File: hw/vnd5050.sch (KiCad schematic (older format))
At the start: 5 parts, among them U401 VND5050AJTR-E

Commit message: making 2.2.0 pcb
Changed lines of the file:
@@
 $Descr A4 11693 8268
 encoding utf-8
-Sheet 6 6
+Sheet 8 8
 Title ""
 Date ""
@@
 AR Path="/5A02A41F/59D8088A" Ref="U901"  Part="1"
 AR Path="/5A07C729/59D8088A" Ref="U901"  Part="1"
-F 0 "U901" H 4700 4447 60  0000 C CNN
+AR Path="/5A337B26/59D8088A" Ref="U801"  Part="1"
+F 0 "U801" H 4700 4447 60  0000 C CNN
 F 1 "VND5050AJTR-E" H 4700 4341 60  0000 C CNN
 F 2 "usevolt:PowerSSO-12" H 4600 4400 60  0001 C CNN
@@
 AR Path="/5A015FC0/59D808C7" Ref="#PWR019"  Part="1"
 AR Path="/5A02A41F/59D808C7" Ref="#PWR029"  Part="1"
-AR Path="/5A07C729/59D808C7" Ref="#PWR602"  Part="1"
-F 0 "#PWR602" H 5250 3500 50  0001 C CNN
+AR Path="/5A07C729/59D808C7" Ref="#PWR502"  Part="1"
+AR Path="/5A337B26/59D808C7" Ref="#PWR702"  Part="1"
+F 0 "#PWR702" H 5250 3500 50  0001 C CNN
 F 1 "VDD" H 5267 3823 50  0000 C CNN
 F 2 "" H 5250 3650 50  0000 C CNN
@@
 AR Path="/5A015FC0/59D86DC2" Ref="#PWR020"  Part="1"
 AR Path="/5A02A41F/59D86DC2" Ref="#PWR030"  Part="1"
-AR Path="/5A07C729/59D86DC2" Ref="#PWR601"  Part="1"
-F 0 "#PWR601" H 3600 4200 50  0001 C CNN
+AR Path="/5A07C729/59D86DC2" Ref="#PWR501"  Part="1"
+AR Path="/5A337B26/59D86DC2" Ref="#PWR701"  Part="1"
+F 0 "#PWR701" H 3600 4200 50  0001 C CNN
 F 1 "GND" H 3605 4277 50  0000 C CNN
 F 2 "" H 3600 4450 50  0000 C CNN
@@
 AR Path="/5A02A41F/59D88771" Ref="R902"  Part="1"
 AR Path="/5A07C729/59D88771" Ref="R902"  Part="1"
-F 0 "R902" H 3850 4284 45  0000 C CNN
+AR Path="/5A337B26/59D88771" Ref="R804"  Part="1"
+F 0 "R804" H 3850 4284 45  0000 C CNN
 F 1 "390" H 3850 4200 45  0000 C CNN
 F 2 "yageo:0603" H 3830 4250 20  0001 C CNN
@@
 AR Path="/5A02A41F/59D88845" Ref="R901"  Part="1"
 AR Path="/5A07C729/59D88845" Ref="R901"  Part="1"
-F 0 "R901" H 3850 4084 45  0000 C CNN
+AR Path="/5A337B26/59D88845" Ref="R803"  Part="1"
+F 0 "R803" H 3850 4084 45  0000 C CNN
 F 1 "390" H 3850 4000 45  0000 C CNN
 F 2 "yageo:0603" H 3830 4050 20  0001 C CNN
@@
 AR Path="/5A02A41F/5A05950C" Ref="R903"  Part="1"
 AR Path="/5A07C729/5A05950C" Ref="R903"  Part="1"
-F 0 "R903" H 3450 4084 45  0000 C CNN
+AR Path="/5A337B26/5A05950C" Ref="R801"  Part="1"
+F 0 "R801" H 3450 4084 45  0000 C CNN
 F 1 "1K" H 3450 4000 45  0000 C CNN
 F 2 "yageo:0603" H 3430 4050 20  0001 C CNN
@@
 AR Path="/5A02A41F/5A059568" Ref="R904"  Part="1"
 AR Path="/5A07C729/5A059568" Ref="R904"  Part="1"
-F 0 "R904" H 3450 4284 45  0000 C CNN
+AR Path="/5A337B26/5A059568" Ref="R802"  Part="1"
+F 0 "R802" H 3450 4284 45  0000 C CNN
 F 1 "1K" H 3450 4200 45  0000 C CNN
 F 2 "yageo:0603" H 3430 4250 20  0001 C CNN

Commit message: 3.0.0 hw with low side heater mosfet
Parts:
- R401, R402: symbol 390 -> fsb-rescue:390
- R403, R404: symbol 1K -> fsb-rescue:1K
- U401: symbol VND5050AJTR-E -> fsb-rescue:VND5050AJTR-E
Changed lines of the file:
@@
-EESchema Schematic File Version 2
-LIBS:fsb-rescue
-LIBS:kemet
-LIBS:power
-LIBS:usevolt
-LIBS:wurth_elektronik_LED
-LIBS:yageo
+EESchema Schematic File Version 4
 LIBS:fsb-cache
 EELAYER 26 0
@@
 SENSE2
 $Comp
-L VND5050AJTR-E U401
+L fsb-rescue:VND5050AJTR-E U401
 U 1 1 59D8088A
 P 4600 4000
@@
 $EndComp
 $Comp
-L VDD #PWR019
+L fsb-rescue:VDD #PWR019
 U 1 1 59D808C7
 P 5250 3650
 AR Path="/5A015FC0/59D808C7" Ref="#PWR019"  Part="1"
 AR Path="/5A02A41F/59D808C7" Ref="#PWR029"  Part="1"
-AR Path="/5A07C729/59D808C7" Ref="#PWR502"  Part="1"
-AR Path="/5A337B26/59D808C7" Ref="#PWR702"  Part="1"
-F 0 "#PWR702" H 5250 3500 50  0001 C CNN
+AR Path="/5A07C729/59D808C7" Ref="#PWR0502"  Part="1"
+AR Path="/5A337B26/59D808C7" Ref="#PWR0702"  Part="1"
+F 0 "#PWR0702" H 5250 3500 50  0001 C CNN
 F 1 "VDD" H 5267 3823 50  0000 C CNN
 F 2 "" H 5250 3650 50  0000 C CNN
@@
 	3200 4000 4300 4000
 $Comp
-L GND #PWR020
+L fsb-rescue:GND #PWR020
 U 1 1 59D86DC2
 P 3600 4450
 AR Path="/5A015FC0/59D86DC2" Ref="#PWR020"  Part="1"
 AR Path="/5A02A41F/59D86DC2" Ref="#PWR030"  Part="1"
-AR Path="/5A07C729/59D86DC2" Ref="#PWR501"  Part="1"
-AR Path="/5A337B26/59D86DC2" Ref="#PWR701"  Part="1"
-F 0 "#PWR701" H 3600 4200 50  0001 C CNN
+AR Path="/5A07C729/59D86DC2" Ref="#PWR0501"  Part="1"
+AR Path="/5A337B26/59D86DC2" Ref="#PWR0701"  Part="1"
+F 0 "#PWR0701" H 3600 4200 50  0001 C CNN
 F 1 "GND" H 3605 4277 50  0000 C CNN
 F 2 "" H 3600 4450 50  0000 C CNN
@@
 	3600 4300 4300 4300
 $Comp
-L 390 R402
+L fsb-rescue:390 R402
 U 1 1 59D88771
 P 3800 4100
@@
 $EndComp
 $Comp
-L 390 R401
+L fsb-rescue:390 R401
 U 1 1 59D88845
 P 3800 3900
@@
 Connection ~ 4150 3900
 $Comp
-L 1K R403
+L fsb-rescue:1K R403
 U 1 1 5A05950C
 P 3400 3900
@@
 $EndComp
 $Comp
-L 1K R404
+L fsb-rescue:1K R404
 U 1 1 5A059568
 P 3400 4100

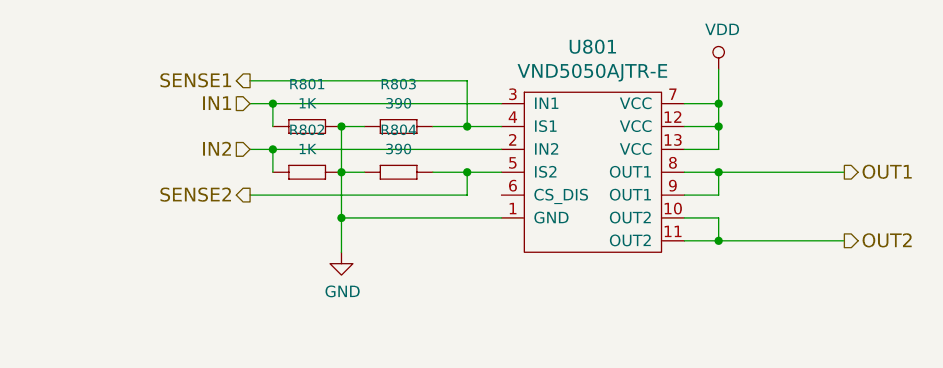
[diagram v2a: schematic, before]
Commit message: HAL updated to latest uv bootloader, starting to draw 6.0.0 pcb
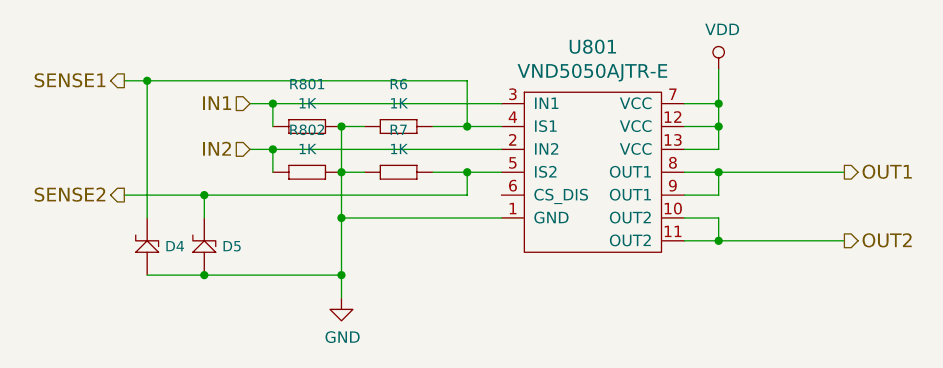
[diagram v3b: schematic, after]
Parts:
- removed R401, R402: 390, yageo:0603, symbol fsb-rescue:390
- added D2, D3: ZENER_MM3Z3V6T1G, usevolt:SOD-323, symbol usevolt:ZENER_MM3Z3V6T1G
- added R1, R2: 1K, yageo:0603, symbol fsb-rescue:1K
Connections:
- net GND: now also D2.2, D3.2, R1.2 (R2), R2.2 (R2)
- net SENSE1: now also D2.1, R1.1 (R1)
- net SENSE2: now also D3.1, R2.1 (R1)
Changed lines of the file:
@@
 $Descr A4 11693 8268
 encoding utf-8
-Sheet 8 8
+Sheet 5 8
 Title ""
 Date ""
@@
 Text HLabel 3200 4000 0    60   Input ~ 0
 IN2
-Text HLabel 3200 3700 0    60   Output ~ 0
+Text HLabel 2650 3700 0    60   Output ~ 0
 SENSE1
-Text HLabel 3200 4200 0    60   Output ~ 0
+Text HLabel 2650 4200 0    60   Output ~ 0
 SENSE2
 $Comp
@@
 $EndComp
 Wire Wire Line
-	5250 3650 5250 4000
+	5250 3650 5250 3800
 Wire Wire Line
 	5250 3800 5100 3800
@@
 Connection ~ 5250 3900
 Wire Wire Line
-	5100 4100 5800 4100
+	5100 4100 5250 4100
 Wire Wire Line
 	5100 4200 5250 4200
@@
 Connection ~ 5250 4100
 Wire Wire Line
-	5100 4400 5800 4400
+	5100 4400 5250 4400
 Wire Wire Line
 	5100 4300 5250 4300
@@
 Connection ~ 5250 4400
 Wire Wire Line
-	3200 3800 4300 3800
-Wire Wire Line
-	3200 4000 4300 4000
+	3200 3800 3300 3800
+Wire Wire Line
+	3200 4000 3300 4000
 $Comp
 L fsb-rescue:GND #PWR020
 U 1 1 59D86DC2
-P 3600 4450
+P 3600 4650
 AR Path="/5A015FC0/59D86DC2" Ref="#PWR020"  Part="1"
 AR Path="/5A02A41F/59D86DC2" Ref="#PWR030"  Part="1"
 AR Path="/5A07C729/59D86DC2" Ref="#PWR0501"  Part="1"
 AR Path="/5A337B26/59D86DC2" Ref="#PWR0701"  Part="1"
-F 0 "#PWR0701" H 3600 4200 50  0001 C CNN
-F 1 "GND" H 3605 4277 50  0000 C CNN
-F 2 "" H 3600 4450 50  0000 C CNN
-F 3 "" H 3600 4450 50  0000 C CNN
-	1    3600 4450
-	1    0    0    -1
-$EndComp
-Wire Wire Line
-	3600 3900 3600 4450
+F 0 "#PWR0701" H 3600 4400 50  0001 C CNN
+F 1 "GND" H 3605 4477 50  0000 C CNN
+F 2 "" H 3600 4650 50  0000 C CNN
+F 3 "" H 3600 4650 50  0000 C CNN
+	1    3600 4650
+	1    0    0    -1
+$EndComp
+Wire Wire Line
+	3600 3900 3600 4100
 Wire Wire Line
 	3600 4300 4300 4300
-$Comp
-L fsb-rescue:390 R402
-U 1 1 59D88771
-P 3800 4100
-AR Path="/5A015FC0/59D88771" Ref="R402"  Part="1"
-AR Path="/5A02A41F/59D88771" Ref="R902"  Part="1"
-AR Path="/5A07C729/59D88771" Ref="R902"  Part="1"
-AR Path="/5A337B26/59D88771" Ref="R804"  Part="1"
-F 0 "R804" H 3850 4284 45  0000 C CNN
-F 1 "390" H 3850 4200 45  0000 C CNN
-F 2 "yageo:0603" H 3830 4250 20  0001 C CNN
-F 3 "" H 3769 4139 60  0001 C CNN
-F 4 "" H 4169 4539 60  0001 C CNN "1st Source Part Number"
-F 5 "Digikey" H 4069 4439 60  0001 C CNN "1st Source"
-F 6 "RC0603FR-07390RL" H 3969 4339 60  0001 C CNN "Manufacturer Part Number"
-F 7 "YAGEO" H 3869 4239 60  0001 C CNN "Manufacturer"
-	1    3800 4100
-	1    0    0    -1
-$EndComp
-$Comp
-L fsb-rescue:390 R401
-U 1 1 59D88845
-P 3800 3900
-AR Path="/5A015FC0/59D88845" Ref="R401"  Part="1"
-AR Path="/5A02A41F/59D88845" Ref="R901"  Part="1"
-AR Path="/5A07C729/59D88845" Ref="R901"  Part="1"
-AR Path="/5A337B26/59D88845" Ref="R803"  Part="1"
-F 0 "R803" H 3850 4084 45  0000 C CNN
-F 1 "390" H 3850 4000 45  0000 C CNN
-F 2 "yageo:0603" H 3830 4050 20  0001 C CNN
-F 3 "" H 3769 3939 60  0001 C CNN
-F 4 "" H 4169 4339 60  0001 C CNN "1st Source Part Number"
-F 5 "Digikey" H 4069 4239 60  0001 C CNN "1st Source"
-F 6 "RC0603FR-07390RL" H 3969 4139 60  0001 C CNN "Manufacturer Part Number"
-F 7 "YAGEO" H 3869 4039 60  0001 C CNN "Manufacturer"
-	1    3800 3900
-	1    0    0    -1
-$EndComp
 Wire Wire Line
 	3700 3900 3600 3900
@@
 Connection ~ 3600 4100
 Wire Wire Line
-	4000 4100 4300 4100
-Wire Wire Line
-	4000 3900 4300 3900
-Wire Wire Line
-	3200 4200 4150 4200
+	4000 4100 4150 4100
+Wire Wire Line
+	4000 3900 4150 3900
+Wire Wire Line
+	2650 4200 3000 4200
 Wire Wire Line
 	4150 4200 4150 4100
@@
 	4150 3900 4150 3700
 Wire Wire Line
-	4150 3700 3200 3700
+	4150 3700 2750 3700
 Connection ~ 4150 3900
 $Comp
@@
 Connection ~ 3300 4000
 Connection ~ 3600 3900
+Wire Wire Line
+	5250 3800 5250 3900
+Wire Wire Line
+	5250 3900 5250 4000
+Wire Wire Line
+	5250 4100 5800 4100
+Wire Wire Line
+	5250 4400 5800 4400
+Wire Wire Line
+	3600 4300 3600 4550
+Wire Wire Line
+	3600 4100 3600 4300
+Wire Wire Line
+	4150 4100 4300 4100
+Wire Wire Line
+	4150 3900 4300 3900
+Wire Wire Line
+	3300 3800 4300 3800
+Wire Wire Line
+	3300 4000 4300 4000
+$Comp
+L fsb-rescue:1K R?
+U 1 1 5C01EA8C
+P 3800 4100
+AR Path="/5A015FC0/5C01EA8C" Ref="R?"  Part="1"
+AR Path="/5A02A41F/5C01EA8C" Ref="R?"  Part="1"
+AR Path="/5A07C729/5C01EA8C" Ref="R2"  Part="1"
+AR Path="/5A337B26/5C01EA8C" Ref="R7"  Part="1"
+F 0 "R7" H 3850 4284 45  0000 C CNN
+F 1 "1K" H 3850 4200 45  0000 C CNN
+F 2 "yageo:0603" H 3830 4250 20  0001 C CNN
+F 3 "" H 3769 4139 60  0001 C CNN
+F 4 "" H 4169 4539 60  0001 C CNN "1st Source Part Number"
+F 5 "Digikey" H 4069 4439 60  0001 C CNN "1st Source"
+F 6 "RC0603FR-071KL" H 3969 4339 60  0001 C CNN "Manufacturer Part Number"
+F 7 "YAGEO" H 3869 4239 60  0001 C CNN "Manufacturer"
+	1    3800 4100
+	1    0    0    -1
+$EndComp
+$Comp
+L fsb-rescue:1K R?
+U 1 1 5C01EABC
+P 3800 3900
+AR Path="/5A015FC0/5C01EABC" Ref="R?"  Part="1"
+AR Path="/5A02A41F/5C01EABC" Ref="R?"  Part="1"
+AR Path="/5A07C729/5C01EABC" Ref="R1"  Part="1"
+AR Path="/5A337B26/5C01EABC" Ref="R6"  Part="1"
+F 0 "R6" H 3850 4084 45  0000 C CNN
+F 1 "1K" H 3850 4000 45  0000 C CNN
+F 2 "yageo:0603" H 3830 4050 20  0001 C CNN
+F 3 "" H 3769 3939 60  0001 C CNN
+F 4 "" H 4169 4339 60  0001 C CNN "1st Source Part Number"
+F 5 "Digikey" H 4069 4239 60  0001 C CNN "1st Source"
+F 6 "RC0603FR-071KL" H 3969 4139 60  0001 C CNN "Manufacturer Part Number"
+F 7 "YAGEO" H 3869 4039 60  0001 C CNN "Manufacturer"
+	1    3800 3900
+	1    0    0    -1
+$EndComp
+$Comp
+L usevolt:ZENER_MM3Z3V6T1G D2
+U 1 1 5C0230BD
+P 2750 4350
+AR Path="/5A07C729/5C0230BD" Ref="D2"  Part="1"
+AR Path="/5A337B26/5C0230BD" Ref="D4"  Part="1"
+F 0 "D4" V 2675 4272 45  0000 R CNN
+F 1 "ZENER_MM3Z3V6T1G" H 3025 4725 45  0001 L BNN
+F 2 "usevolt:SOD-323" H 2725 4725 20  0001 C CNN
+F 3 "http://www.mouser.com/ds/2/308/MM3Z2V4T1-D-269162.pdf" H 3100 4925 60  0001 C CNN
+F 4 "Mouser" H 3070 4670 60  0001 C CNN "1st Source"
+F 5 "MM3Z3V6T1G" H 2970 4570 60  0001 C CNN "Manufacturer Part Number"
+F 6 "863-MM3Z3V6T1G" H 3170 4770 60  0001 C CNN "1st Source Part Number"
+F 7 "ON Semiconductor" H 3025 4825 60  0001 C CNN "Manufacturer"
+	1    2750 4350
+	0    -1   -1   0
+$EndComp
+$Comp
+L usevolt:ZENER_MM3Z3V6T1G D3
+U 1 1 5C023146
+P 3000 4350
+AR Path="/5A07C729/5C023146" Ref="D3"  Part="1"
+AR Path="/5A337B26/5C023146" Ref="D5"  Part="1"
+F 0 "D5" V 2925 4272 45  0000 R CNN
+F 1 "ZENER_MM3Z3V6T1G" H 3275 4725 45  0001 L BNN
+F 2 "usevolt:SOD-323" H 2975 4725 20  0001 C CNN
+F 3 "http://www.mouser.com/ds/2/308/MM3Z2V4T1-D-269162.pdf" H 3350 4925 60  0001 C CNN
+F 4 "Mouser" H 3320 4670 60  0001 C CNN "1st Source"
+F 5 "MM3Z3V6T1G" H 3220 4570 60  0001 C CNN "Manufacturer Part Number"
+F 6 "863-MM3Z3V6T1G" H 3420 4770 60  0001 C CNN "1st Source Part Number"
+F 7 "ON Semiconductor" H 3275 4825 60  0001 C CNN "Manufacturer"
+	1    3000 4350
+	0    -1   -1   0
+$EndComp
+Wire Wire Line
+	3000 4300 3000 4200
+Connection ~ 3000 4200
+Wire Wire Line
+	3000 4200 4150 4200
+Wire Wire Line
+	2750 4300 2750 3700
+Connection ~ 2750 3700
+Wire Wire Line
+	2750 3700 2650 3700
+Wire Wire Line
+	2750 4550 3000 4550
+Wire Wire Line
+	3000 4550 3600 4550
+Connection ~ 3000 4550
+Connection ~ 3600 4550
+Wire Wire Line
+	3600 4550 3600 4650
 $EndSCHEMATC

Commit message: coolvalve added to fsb
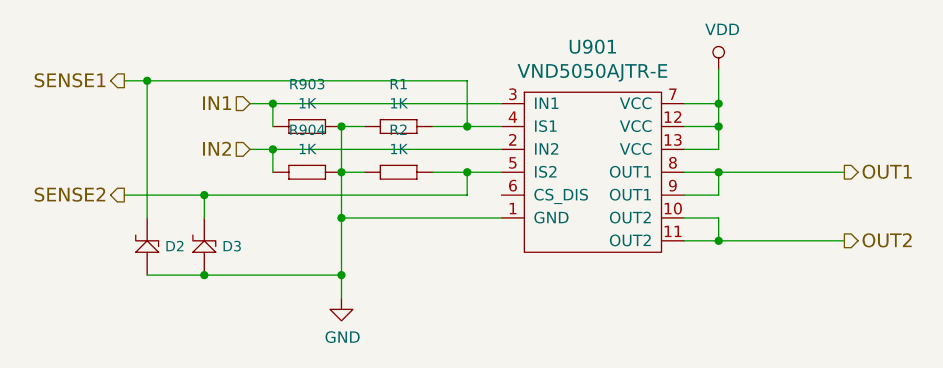
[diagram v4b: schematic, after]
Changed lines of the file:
@@
 $Descr A4 11693 8268
 encoding utf-8
-Sheet 5 8
+Sheet 5 9
 Title ""
 Date ""
@@
 AR Path="/5A07C729/59D8088A" Ref="U901"  Part="1"
 AR Path="/5A337B26/59D8088A" Ref="U801"  Part="1"
-F 0 "U801" H 4700 4447 60  0000 C CNN
+AR Path="/5F353556/59D8088A" Ref="U4"  Part="1"
+F 0 "U901" H 4700 4447 60  0000 C CNN
 F 1 "VND5050AJTR-E" H 4700 4341 60  0000 C CNN
 F 2 "usevolt:PowerSSO-12" H 4600 4400 60  0001 C CNN
@@
 AR Path="/5A07C729/59D808C7" Ref="#PWR0502"  Part="1"
 AR Path="/5A337B26/59D808C7" Ref="#PWR0702"  Part="1"
-F 0 "#PWR0702" H 5250 3500 50  0001 C CNN
+AR Path="/5F353556/59D808C7" Ref="#PWR0116"  Part="1"
+F 0 "#PWR0502" H 5250 3500 50  0001 C CNN
 F 1 "VDD" H 5267 3823 50  0000 C CNN
 F 2 "" H 5250 3650 50  0000 C CNN
@@
 AR Path="/5A07C729/59D86DC2" Ref="#PWR0501"  Part="1"
 AR Path="/5A337B26/59D86DC2" Ref="#PWR0701"  Part="1"
-F 0 "#PWR0701" H 3600 4400 50  0001 C CNN
+AR Path="/5F353556/59D86DC2" Ref="#PWR0117"  Part="1"
+F 0 "#PWR0501" H 3600 4400 50  0001 C CNN
 F 1 "GND" H 3605 4477 50  0000 C CNN
 F 2 "" H 3600 4650 50  0000 C CNN
@@
 AR Path="/5A07C729/5A05950C" Ref="R903"  Part="1"
 AR Path="/5A337B26/5A05950C" Ref="R801"  Part="1"
-F 0 "R801" H 3450 4084 45  0000 C CNN
+AR Path="/5F353556/5A05950C" Ref="R15"  Part="1"
+F 0 "R903" H 3450 4084 45  0000 C CNN
 F 1 "1K" H 3450 4000 45  0000 C CNN
 F 2 "yageo:0603" H 3430 4050 20  0001 C CNN
@@
 AR Path="/5A07C729/5A059568" Ref="R904"  Part="1"
 AR Path="/5A337B26/5A059568" Ref="R802"  Part="1"
-F 0 "R802" H 3450 4284 45  0000 C CNN
+AR Path="/5F353556/5A059568" Ref="R16"  Part="1"
+F 0 "R904" H 3450 4284 45  0000 C CNN
 F 1 "1K" H 3450 4200 45  0000 C CNN
 F 2 "yageo:0603" H 3430 4250 20  0001 C CNN
@@
 AR Path="/5A07C729/5C01EA8C" Ref="R2"  Part="1"
 AR Path="/5A337B26/5C01EA8C" Ref="R7"  Part="1"
-F 0 "R7" H 3850 4284 45  0000 C CNN
+AR Path="/5F353556/5C01EA8C" Ref="R18"  Part="1"
+F 0 "R2" H 3850 4284 45  0000 C CNN
 F 1 "1K" H 3850 4200 45  0000 C CNN
 F 2 "yageo:0603" H 3830 4250 20  0001 C CNN
@@
 AR Path="/5A07C729/5C01EABC" Ref="R1"  Part="1"
 AR Path="/5A337B26/5C01EABC" Ref="R6"  Part="1"
-F 0 "R6" H 3850 4084 45  0000 C CNN
+AR Path="/5F353556/5C01EABC" Ref="R17"  Part="1"
+F 0 "R1" H 3850 4084 45  0000 C CNN
 F 1 "1K" H 3850 4000 45  0000 C CNN
 F 2 "yageo:0603" H 3830 4050 20  0001 C CNN
@@
 AR Path="/5A07C729/5C0230BD" Ref="D2"  Part="1"
 AR Path="/5A337B26/5C0230BD" Ref="D4"  Part="1"
-F 0 "D4" V 2675 4272 45  0000 R CNN
+AR Path="/5F353556/5C0230BD" Ref="D8"  Part="1"
+F 0 "D2" V 2675 4272 45  0000 R CNN
 F 1 "ZENER_MM3Z3V6T1G" H 3025 4725 45  0001 L BNN
 F 2 "usevolt:SOD-323" H 2725 4725 20  0001 C CNN
@@
 AR Path="/5A07C729/5C023146" Ref="D3"  Part="1"
 AR Path="/5A337B26/5C023146" Ref="D5"  Part="1"
-F 0 "D5" V 2925 4272 45  0000 R CNN
+AR Path="/5F353556/5C023146" Ref="D9"  Part="1"
+F 0 "D3" V 2925 4272 45  0000 R CNN
 F 1 "ZENER_MM3Z3V6T1G" H 3275 4725 45  0001 L BNN
 F 2 "usevolt:SOD-323" H 2975 4725 20  0001 C CNN
